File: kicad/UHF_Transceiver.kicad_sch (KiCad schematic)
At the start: 24 parts

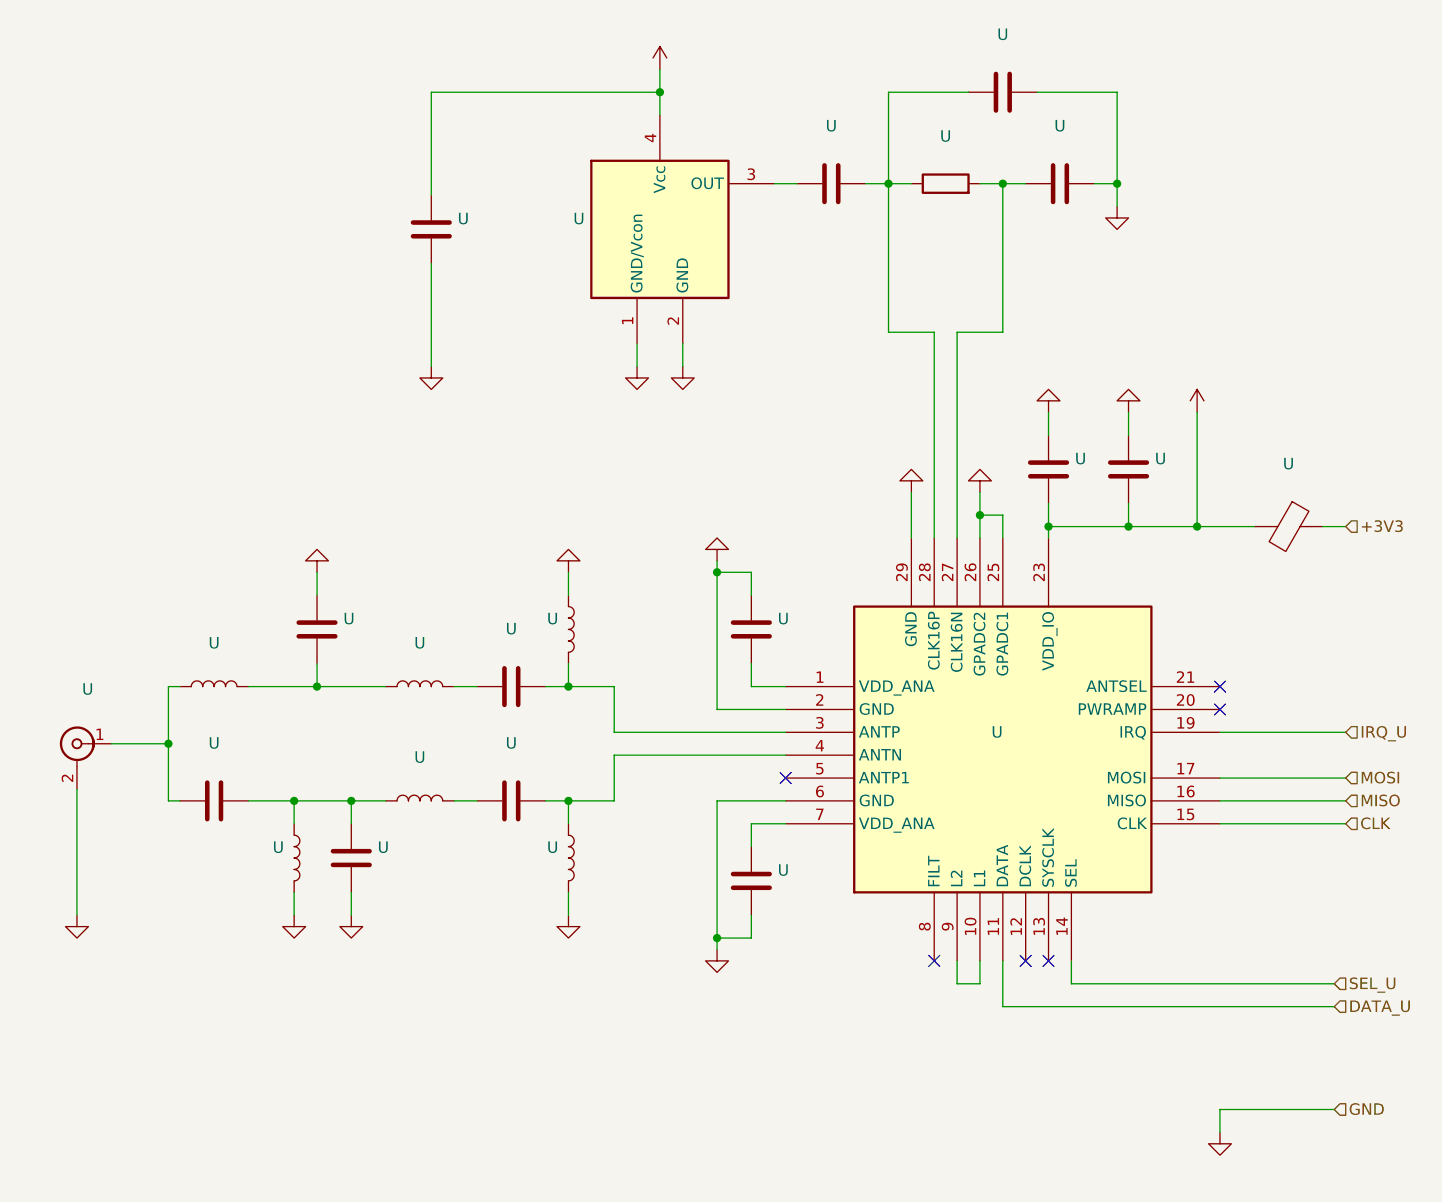
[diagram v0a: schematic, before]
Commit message: Adding PIB USB BRIDGE UML state diagrams - WIP
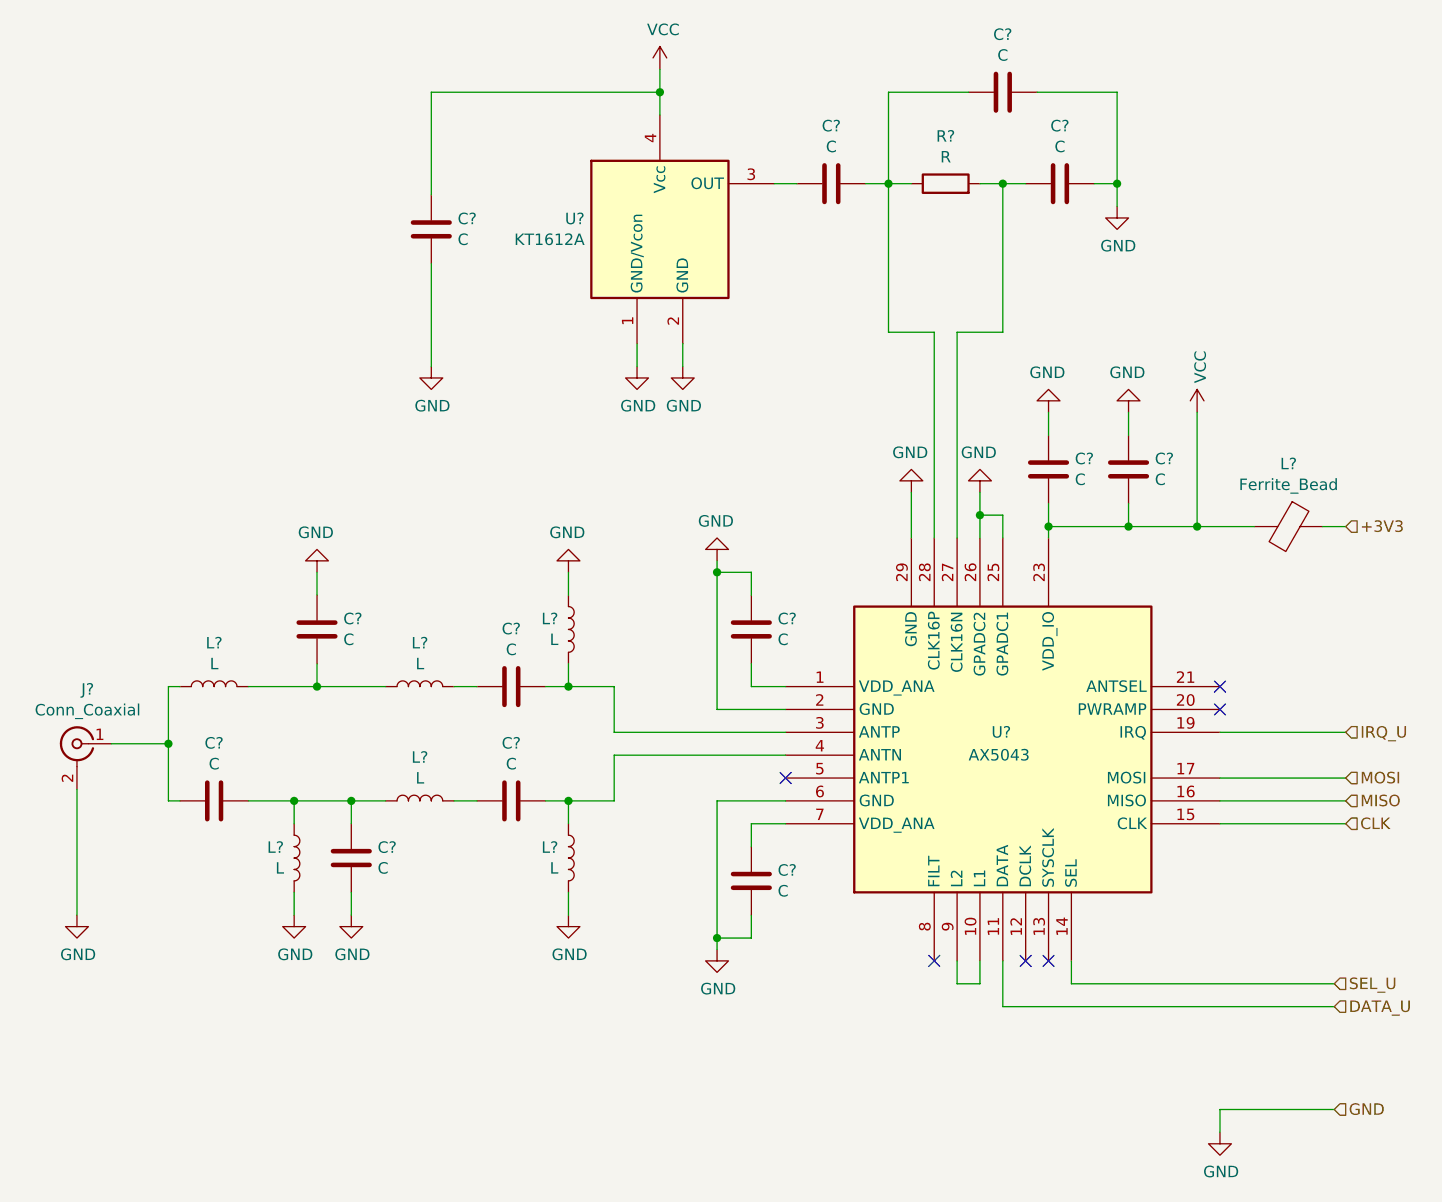
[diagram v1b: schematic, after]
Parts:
- C? (x13): renamed from U; value (none) -> C; symbol device:C -> RCTX-rescue:C-device
- J?: renamed from U; value (none) -> Conn_Coaxial; symbol conn:Conn_Coaxial -> RCTX-rescue:Conn_Coaxial-conn
- L? (x6): renamed from U; value (none) -> L; symbol device:L -> RCTX-rescue:L-device
- L?: renamed from U; value (none) -> Ferrite_Bead; symbol device:Ferrite_Bead -> RCTX-rescue:Ferrite_Bead-device
- R?: renamed from U; value (none) -> R; symbol device:R -> RCTX-rescue:R-device
- U?: renamed from U; value (none) -> AX5043; footprint (none) -> Housings_DFN_QFN:QFN-28-1EP_5x5mm_Pitch0.5mm; symbol AX5043:AX5043 -> RCTX-rescue:AX5043-AX5043
- U?: renamed from U; value (none) -> KT1612A; footprint (none) -> lsf-kicad-lib:KT1612; symbol KT1612a:KT1612A -> RCTX-rescue:KT1612A-KT1612a
